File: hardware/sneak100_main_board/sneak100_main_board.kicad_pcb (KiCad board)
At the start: 2 copper layers, 50 x 72 mm, 63 parts, among them J1 Conn_02x05_Counter_Clockwise, J10 Conn_01x03, J2 Conn_01x03, J3 Conn_01x06, J4 Conn_01x06, J5 Conn_01x06, J6 Conn_01x06, J7 Conn_01x03, J8 Conn_01x03, J9 Conn_01x03, Q1 SFH-313FA, Q2 SFH-313FA, Q3 SFH-313FA, Q4 SFH-313FA, Q5 SFH-313FA, Q6 SFH-313FA, SW1 SW_Push, SW2 SW_Push, U1 DRV8835, U2 DRV8835, U3 DRV8835, U4 DRV8835, U5 CD4051B, U6 CD4051B

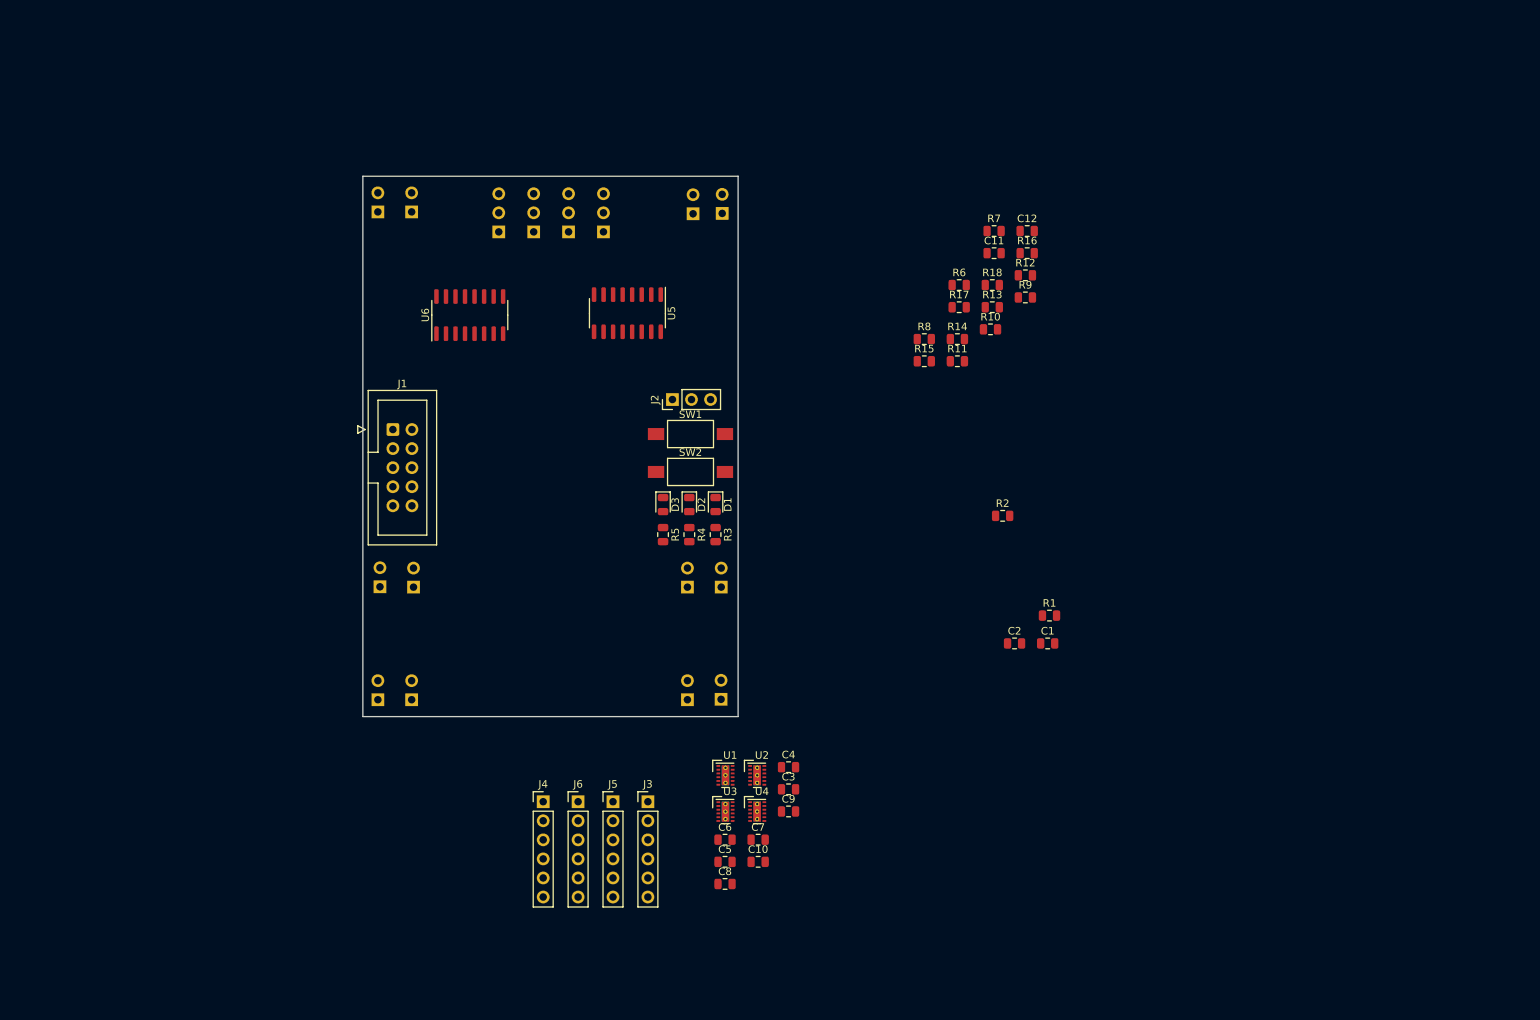
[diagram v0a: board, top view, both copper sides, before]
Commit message: Add stm32f405 uC scheme
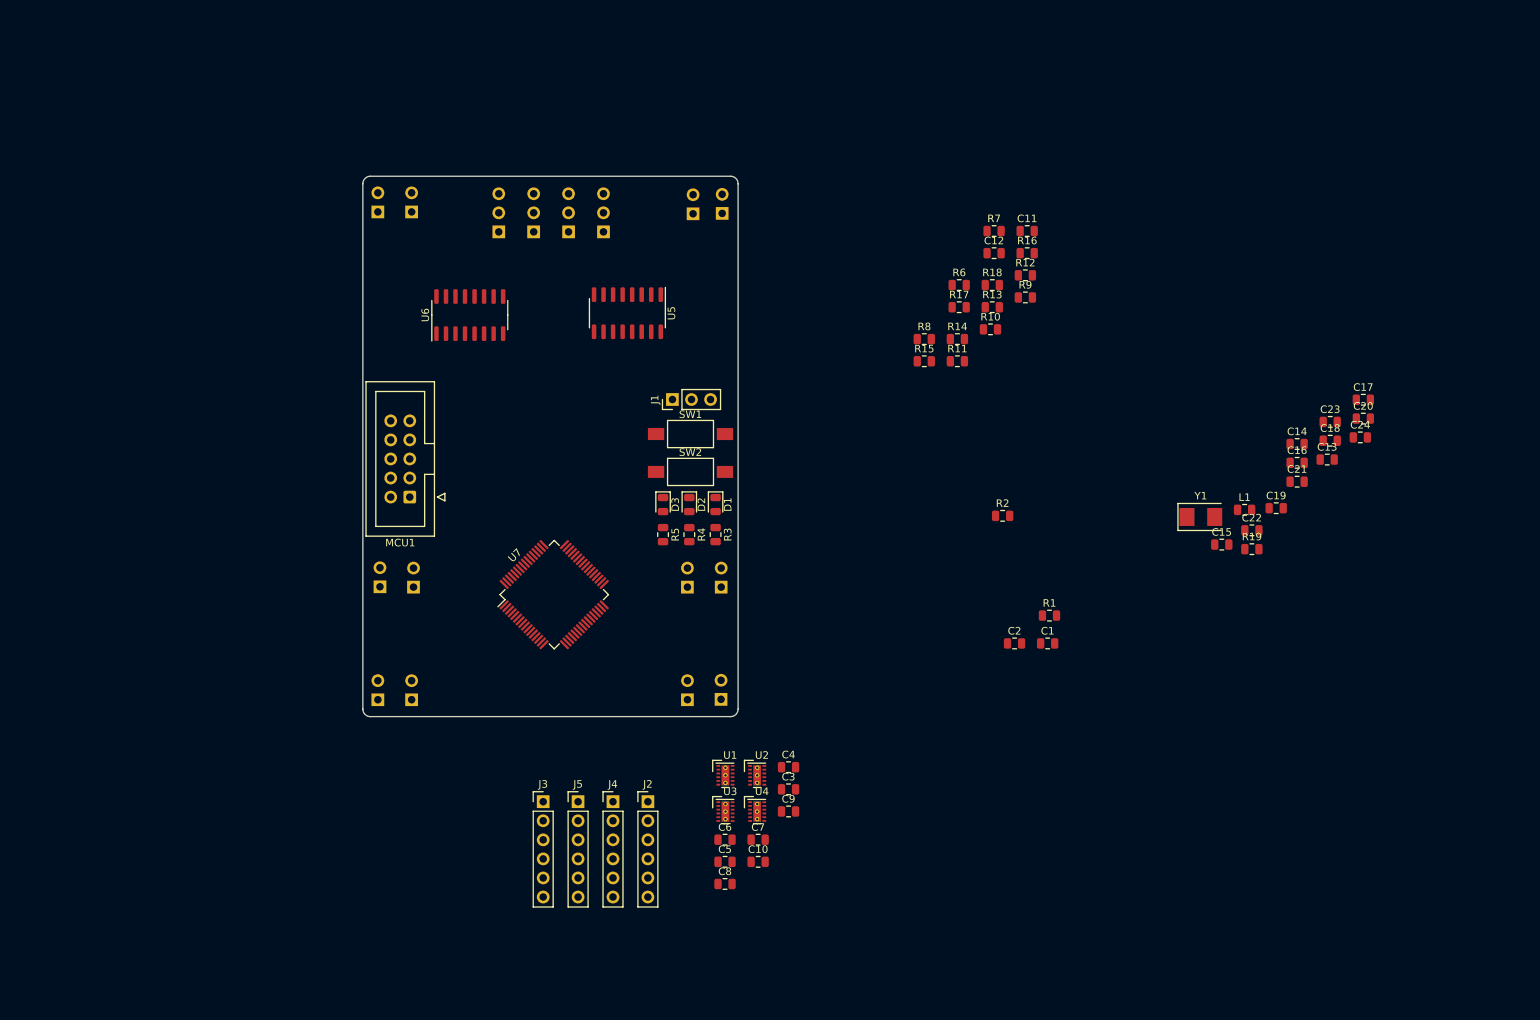
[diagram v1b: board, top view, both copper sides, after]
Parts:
- removed the J1 at (126.8, 75.2)
- added C13: 100nF, Capacitor_SMD:C_0805_2012Metric, F.Cu at (251.2, 79.2)
- added C14: 2.2uF, Capacitor_SMD:C_0805_2012Metric, F.Cu at (247.2, 77.2)
- added C15: 2.2uF, Capacitor_SMD:C_0805_2012Metric, F.Cu at (237.2, 90.6)
- added C16: 1uF, Capacitor_SMD:C_0805_2012Metric, F.Cu at (247.2, 79.7)
- added C17: 100nF, Capacitor_SMD:C_0805_2012Metric, F.Cu at (256.1, 71.3)
- added C18: 20pF, Capacitor_SMD:C_0805_2012Metric, F.Cu at (251.7, 76.7)
- added C19: 20pF, Capacitor_SMD:C_0805_2012Metric, F.Cu at (244.4, 85.7)
- added C20: 100nF, Capacitor_SMD:C_0805_2012Metric, F.Cu at (256.1, 73.8)
- added C21: 100nF, Capacitor_SMD:C_0805_2012Metric, F.Cu at (247.2, 82.2)
- added C22: 100nF, Capacitor_SMD:C_0805_2012Metric, F.Cu at (241.2, 88.7)
- added C23: 100nF, Capacitor_SMD:C_0805_2012Metric, F.Cu at (251.7, 74.2)
- added C24: 4.7uF, Capacitor_SMD:C_0805_2012Metric, F.Cu at (255.7, 76.3)
- added L1: 4.7uH, Inductor_SMD:L_0805_2012Metric, F.Cu at (240.2, 86.0)
- added MCU1: Conn_02x05_Counter_Clockwise, Connector_IDC:IDC-Header_2x05_P2.54mm_Vertical, F.Cu at (129.0, 84.2)
- added R19: 10k, Resistor_SMD:R_0805_2012Metric, F.Cu at (241.2, 91.2)
- added U7: STM32F405RGTx, Package_QFP:LQFP-64_10x10mm_P0.5mm, F.Cu at (148.2, 97.2)
- added Y1: 8MHz, Crystal:Crystal_SMD_5032-2Pin_5.0x3.2mm, F.Cu at (234.4, 86.9)
- renumbered C12 to C11, C11 to C12, J2 to J1, J3 to J2, J4 to J3, J5 to J4, J6 to J5, J7 to J6, J8 to J7, J9 to J8, J10 to J9
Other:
- outline, holes or cut-outs redrawn

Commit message: Hardware configuration schematic
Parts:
- added C3: 4.7uF, Capacitor_SMD:CP_Elec_4x3, F.Cu at (250.2, 102.2)
- added J2: Conn_01x06, Connector_PinSocket_2.54mm:PinSocket_1x06_P2.54mm_Vertical, F.Cu at (229.1, 101.7)
- added J3: Conn_01x04, Connector_PinSocket_2.54mm:PinSocket_1x04_P2.54mm_Vertical, F.Cu at (233.7, 101.7)
- added J4: Conn_01x02, Connector_PinHeader_2.54mm:PinHeader_1x02_P2.54mm_Vertical, F.Cu at (248.7, 107.5)
- added R24: 4k7, Resistor_SMD:R_0805_2012Metric, F.Cu at (234.5, 80.2)
- added R25: 4k7, Resistor_SMD:R_0805_2012Metric, F.Cu at (238.9, 80.2)
- added R6: 100, Resistor_SMD:R_0805_2012Metric, F.Cu at (233.5, 113.0)
- added R7: 10k, Resistor_SMD:R_0805_2012Metric, F.Cu at (242.8, 108.3)
- added R8: 22, Resistor_SMD:R_0805_2012Metric, F.Cu at (242.8, 111.3)
- added R9: 22, Resistor_SMD:R_0805_2012Metric, F.Cu at (256.3, 100.8)
- added U1: TSOP4838, Connector_PinHeader_2.54mm:PinHeader_1x03_P2.54mm_Vertical, F.Cu at (238.2, 109.2)
- J1: value Conn_01x03 -> USB_OTG; footprint Connector_PinHeader_2.54mm:PinHeader_1x03_P2.54mm_Vertical -> Connector_USB:USB_Micro-B_Molex_47346-0001
- moved J1 42.5 mm to (148.2, 110.8), turned to 0 degrees
- moved D9 25.6 mm to (195.0, 118.5)
- moved Q6 25.6 mm to (190.5, 118.5)
- moved D8 19.2 mm to (106.5, 117.2)
- moved Q5 19.2 mm to (111.0, 117.2)
- moved C11 16.7 mm to (160.2, 139.6)
- moved C4 16.7 mm to (164.2, 129.9)
- moved C5 16.7 mm to (164.2, 127.0)
- moved C6 16.7 mm to (155.8, 139.6)
- moved C7 16.7 mm to (155.8, 136.7)
- moved C8 16.7 mm to (160.2, 136.7)
- moved C9 16.7 mm to (155.8, 142.6)
- moved J5 16.7 mm to (145.5, 131.6)
- moved J6 16.7 mm to (131.5, 131.6)
- moved J7 16.7 mm to (140.8, 131.6)
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- renumbered C9 to C10, C10 to C11, C11 to C12, C12 to C13, C13 to C14, C14 to C15, C15 to C16, C16 to C17, C17 to C18, C18 to C19, C19 to C20, C20 to C21, C21 to C22, C22 to C23, C23 to C24, C24 to C25, C3 to C4, C4 to C5, C5 to C6, C6 to C7, C7 to C8, C8 to C9, J7 to J10, J8 to J11, J9 to J12, J2 to J5, J3 to J6, J4 to J7, J5 to J8, J6 to J9, R3 to R1, R6 to R10, R7 to R11, R8 to R12, R9 to R13, R10 to R14, R11 to R15, R12 to R16, R13 to R17, R14 to R18, R15 to R19, R1 to R2, R16 to R20, R17 to R21, R18 to R22, R19 to R23, R2 to R3, U1 to U2, U2 to U3, U3 to U4, U4 to U5, U5 to U6, U6 to U7, U7 to U8
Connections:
- C14 pad 1: /controller/RESET -> /interface/BUTTON2
- J1 pad 2: (no net) -> Net-(J1-Pad2)
- J1 pad 3: GND -> Net-(J1-Pad3)
- J10 pad 1: (no net) -> /controller/LINE_LM
- J11 pad 1: (no net) -> /controller/LINE_RM
- J12 pad 1: (no net) -> /controller/LINE_RR
- J5 pad 2: (no net) -> /controller/LF_B
- J5 pad 3: (no net) -> /controller/LF_A
- J6 pad 2: (no net) -> /controller/RF_B
- J6 pad 3: (no net) -> /controller/RF_A
- J7 pad 2: (no net) -> /controller/LB_B
- J7 pad 3: (no net) -> /controller/LB_A
- J8 pad 2: (no net) -> /controller/RB_B
- J8 pad 3: (no net) -> /controller/RB_A
- J9 pad 1: (no net) -> /controller/LINE_LL
- MCU1 pad 1: /controller/RESET -> /interface/BUTTON2
- R1 pad 2: (no net) -> /interface/LED1
- R22 pad 1: /proximitySensors/TX_ENABLE -> /controller/PROXIMITY_TX_ENABLE
- R23 pad 2: /controller/RESET -> /interface/BUTTON2
- R4 pad 2: (no net) -> /interface/LED2
- R5 pad 2: (no net) -> /interface/LED3
- U2 pad 10: /motors/LF_IN1 -> /controller/LF_IN1
- U2 pad 7: /motors/LF_IN2 -> /controller/LF_IN2
- U2 pad 8: /motors/LF_IN1 -> /controller/LF_IN1
- U2 pad 9: /motors/LF_IN2 -> /controller/LF_IN2
- U3 pad 10: /motors/RF_IN1 -> /controller/RF_IN1
- U3 pad 7: /motors/RF_IN2 -> /controller/RF_IN2
- U3 pad 8: /motors/RF_IN1 -> /controller/RF_IN1
- U3 pad 9: /motors/RF_IN2 -> /controller/RF_IN2
- U4 pad 10: /motors/LB_IN1 -> /controller/LB_IN1
- U4 pad 7: /motors/LB_IN2 -> /controller/LB_IN2
- U4 pad 8: /motors/LB_IN1 -> /controller/LB_IN1
- U4 pad 9: /motors/LB_IN2 -> /controller/LB_IN2
- U5 pad 10: /motors/RB_IN1 -> /controller/RB_IN1
- U5 pad 7: /motors/RB_IN2 -> /controller/RB_IN2
- U5 pad 8: /motors/RB_IN1 -> /controller/RB_IN1
- U5 pad 9: /motors/RB_IN2 -> /controller/RB_IN2
- U6 pad 6: /proximitySensors/TX_ENABLE -> /controller/PROXIMITY_TX_ENABLE
- U7 pad 3: (no net) -> /controller/PROXIMITY_RX_READ
- U8 pad 10: (no net) -> /controller/LINE_RM
- U8 pad 11: (no net) -> /controller/LINE_RR
- U8 pad 14: (no net) -> /controller/RF_A
- U8 pad 15: (no net) -> /controller/RF_B
- U8 pad 16: (no net) -> /interface/BLUETOOTH_RX
- U8 pad 17: (no net) -> /interface/BLUETOOTH_TX
- U8 pad 2: (no net) -> /controller/MODULE_START
- U8 pad 22: (no net) -> /controller/LB_A
- U8 pad 23: (no net) -> /controller/LB_B
- U8 pad 25: (no net) -> /controller/PROXIMITY_RX_READ
- U8 pad 26: (no net) -> /controller/LB_IN1
- U8 pad 27: (no net) -> /controller/LB_IN2
- U8 pad 29: (no net) -> /controller/RF_IN1
- U8 pad 3: (no net) -> /controller/MODULE_KILL
- U8 pad 30: (no net) -> /controller/RF_IN2
- U8 pad 35: (no net) -> /controller/LF_IN1
- U8 pad 36: (no net) -> /controller/LF_IN2
- U8 pad 37: (no net) -> /controller/LF_A
- U8 pad 38: (no net) -> /controller/LF_B
- U8 pad 39: (no net) -> /controller/PROXIMITY_TX_ENABLE
- U8 pad 40: (no net) -> /controller/I2C3_SDA
- U8 pad 41: (no net) -> /controller/I2C3_SCL
- U8 pad 44: (no net) -> /controller/USB_DM
- U8 pad 45: (no net) -> /controller/USB_DP
- U8 pad 50: (no net) -> /interface/LED1
- U8 pad 51: (no net) -> /interface/LED2
- U8 pad 52: (no net) -> /interface/LED3
- U8 pad 53: (no net) -> /interface/BUTTON1
- U8 pad 54: (no net) -> /controller/RECEIVER_OUT
- U8 pad 55: (no net) -> /proximitySensors/ADD0
- U8 pad 56: (no net) -> /proximitySensors/ADD1
- U8 pad 57: (no net) -> /proximitySensors/ADD2
- U8 pad 58: (no net) -> /controller/RB_A
- U8 pad 59: (no net) -> /controller/RB_B
- U8 pad 61: (no net) -> /controller/RB_IN1
- U8 pad 62: (no net) -> /controller/RB_IN2
- U8 pad 7: /controller/RESET -> /interface/BUTTON2
- U8 pad 8: (no net) -> /controller/LINE_LL
- U8 pad 9: (no net) -> /controller/LINE_LM

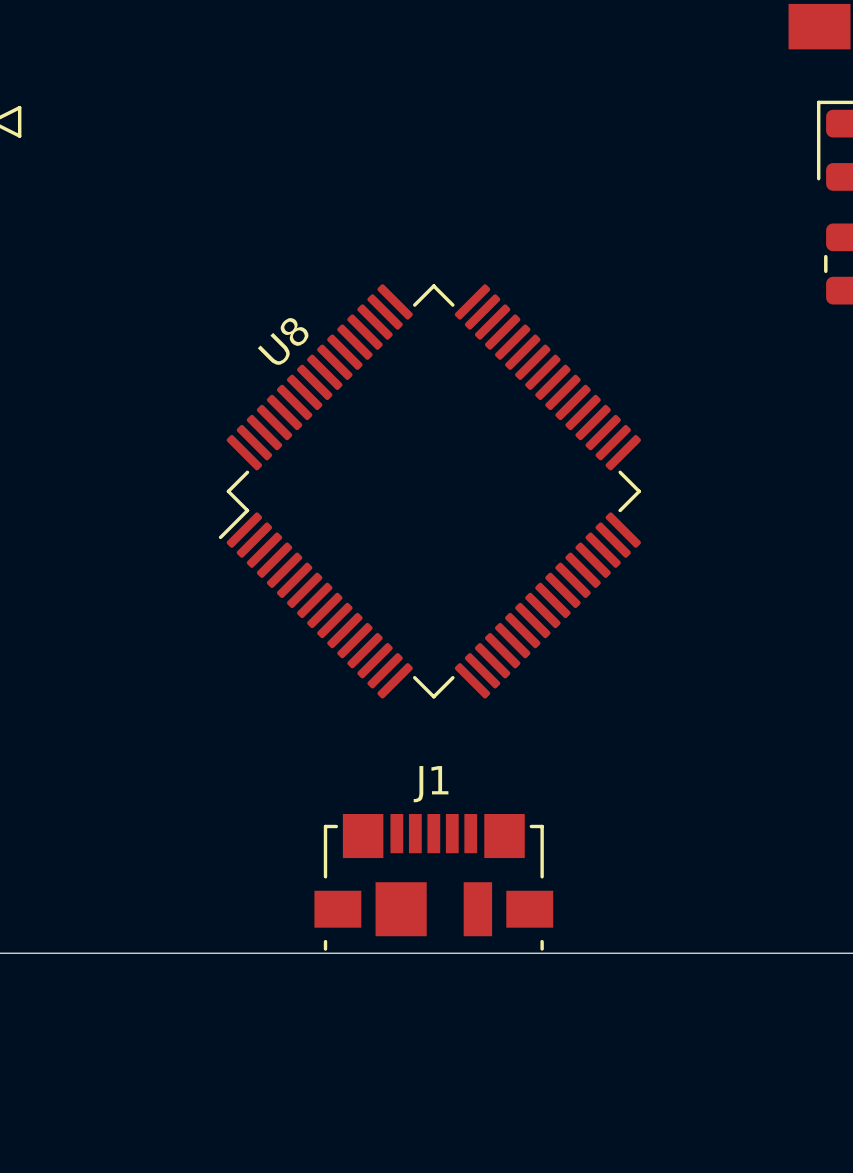
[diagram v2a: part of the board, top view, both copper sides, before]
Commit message: Change usb connector footprint
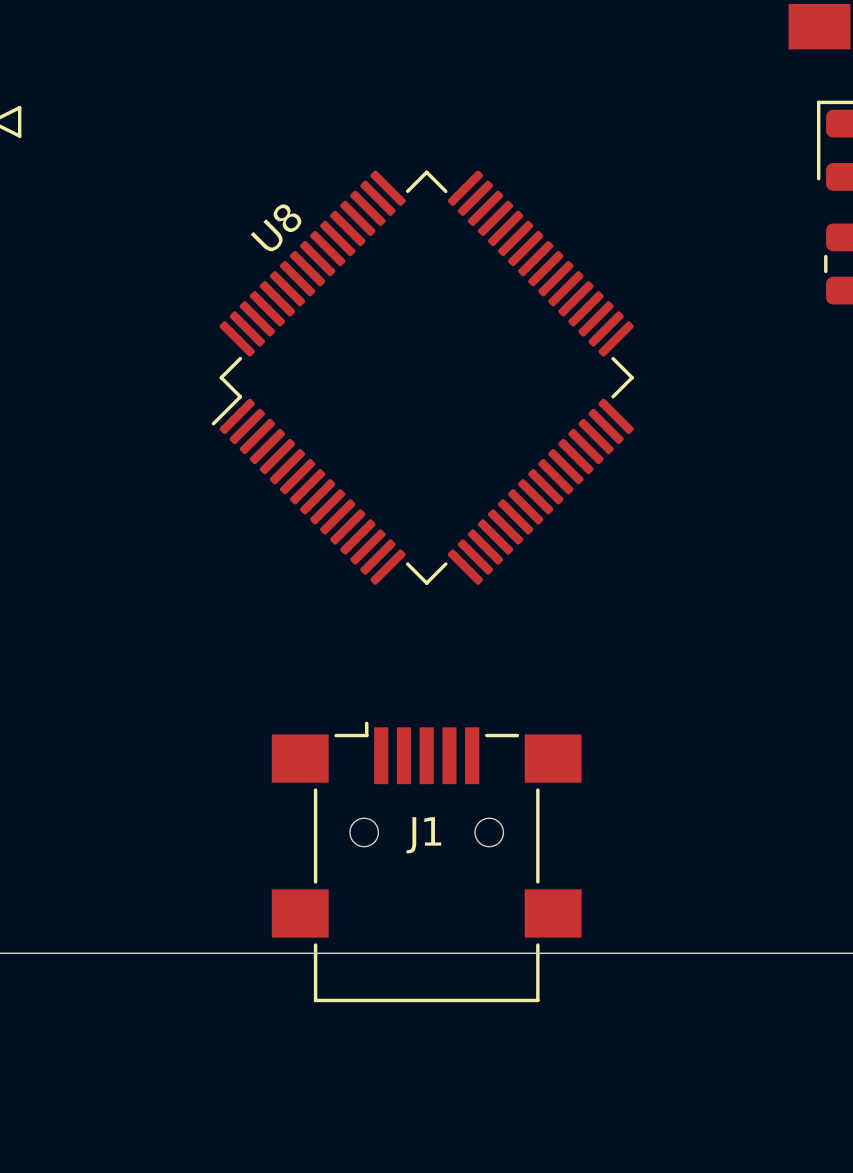
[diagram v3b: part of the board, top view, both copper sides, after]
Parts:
- J1: footprint Connector_USB:USB_Micro-B_Molex_47346-0001 -> Connector_USB:USB_Mini-B_Lumberg_2486_01_Horizontal
- moved U8 4.01 mm to (148.0, 93.2)
- moved J1 1.52 mm to (148.0, 109.2)

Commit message: Power section scheme
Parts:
- added C12: 100nF, Capacitor_SMD:C_0603_1608Metric, F.Cu at (251.8, 59.2)
- added C13: 4.7uF, Capacitor_SMD:CP_Elec_4x3, F.Cu at (243.7, 49.2)
- added C14: 4.7uF, Capacitor_SMD:CP_Elec_4x3, F.Cu at (237.8, 59.0)
- added C15: 100nF, Capacitor_SMD:C_0603_1608Metric, F.Cu at (255.8, 57.2)
- added D4: LED, LED_SMD:LED_0603_1608Metric, F.Cu at (254.2, 47.5)
- added D5: LED, LED_SMD:LED_0603_1608Metric, F.Cu at (243.7, 57.9)
- added D6: LED, LED_SMD:LED_0603_1608Metric, F.Cu at (236.0, 63.2)
- added J10: Conn_01x02, Connector_PinHeader_2.54mm:PinHeader_1x02_P2.54mm_Vertical, F.Cu at (249.9, 48.6)
- added J9: Conn_01x03, Connector_PinHeader_2.54mm:PinHeader_1x03_P2.54mm_Vertical, F.Cu at (237.5, 48.6)
- added Q1: Q_PMOS_DGS, Package_TO_SOT_SMD:SOT-23, F.Cu at (243.9, 54.4)
- added Q2: Q_PMOS_DGS, Package_TO_SOT_SMD:SOT-23, F.Cu at (248.4, 55.7)
- added R10: 4k7, Resistor_SMD:R_0603_1608Metric, F.Cu at (244.0, 63.0)
- added R11: 1k, Resistor_SMD:R_0603_1608Metric, F.Cu at (252.6, 54.7)
- added R12: 1k, Resistor_SMD:R_0603_1608Metric, F.Cu at (240.0, 63.1)
- added R13: R, Resistor_SMD:R_0603_1608Metric, F.Cu at (243.7, 60.5)
- added R14: 1.5k, Resistor_SMD:R_0603_1608Metric, F.Cu at (254.2, 50.1)
- added R15: 680, Resistor_SMD:R_0603_1608Metric, F.Cu at (247.7, 59.2)
- added R16: 340, Resistor_SMD:R_0603_1608Metric, F.Cu at (248.0, 61.8)
- added R17: R, Resistor_SMD:R_0603_1608Metric, F.Cu at (252.0, 61.8)
- added SW3: SW_Push_SPDT, Button_Switch_SMD:SW_SPDT_CK-JS102011SAQN, F.Cu at (229.6, 51.3)
- added U6: LM1117-3.3, Package_TO_SOT_SMD:SOT-223-3_TabPin2, F.Cu at (229.0, 60.2)
- C1, C10, C11, C2, C4, C5, C6, C7, C8, C9: footprint Capacitor_SMD:C_0805_2012Metric -> Capacitor_SMD:C_0603_1608Metric
- C16: renamed from C12; footprint Capacitor_SMD:C_0805_2012Metric -> Capacitor_SMD:C_0603_1608Metric
- C17: renamed from C13; footprint Capacitor_SMD:C_0805_2012Metric -> Capacitor_SMD:C_0603_1608Metric
- C18: renamed from C14; footprint Capacitor_SMD:C_0805_2012Metric -> Capacitor_SMD:C_0603_1608Metric
- C19: renamed from C15; footprint Capacitor_SMD:C_0805_2012Metric -> Capacitor_SMD:C_0603_1608Metric
- C20: renamed from C16; footprint Capacitor_SMD:C_0805_2012Metric -> Capacitor_SMD:C_0603_1608Metric
- C21: renamed from C17; footprint Capacitor_SMD:C_0805_2012Metric -> Capacitor_SMD:C_0603_1608Metric
- C22: renamed from C18; footprint Capacitor_SMD:C_0805_2012Metric -> Capacitor_SMD:C_0603_1608Metric
- C23: renamed from C19; footprint Capacitor_SMD:C_0805_2012Metric -> Capacitor_SMD:C_0603_1608Metric
- C24: renamed from C20; footprint Capacitor_SMD:C_0805_2012Metric -> Capacitor_SMD:C_0603_1608Metric
- C25: renamed from C21; footprint Capacitor_SMD:C_0805_2012Metric -> Capacitor_SMD:C_0603_1608Metric
- C26: renamed from C22; footprint Capacitor_SMD:C_0805_2012Metric -> Capacitor_SMD:C_0603_1608Metric
- C27: renamed from C23; footprint Capacitor_SMD:C_0805_2012Metric -> Capacitor_SMD:C_0603_1608Metric
- C28: renamed from C24; footprint Capacitor_SMD:C_0805_2012Metric -> Capacitor_SMD:C_0603_1608Metric
- D1, D2, D3: footprint LED_SMD:LED_0805_2012Metric -> LED_SMD:LED_0603_1608Metric
- renumbered C25 to C29, D7 to D10, D8 to D11, D9 to D12, D4 to D7, D5 to D8, D6 to D9, J9 to J11, J10 to J12, J11 to J13, J12 to J14, Q1 to Q3, Q2 to Q4, Q3 to Q5, Q4 to Q6, Q5 to Q7, Q6 to Q8, R10 to R18, R11 to R19, R12 to R20, R13 to R21, R14 to R22, R15 to R23, R16 to R24, R17 to R25, R18 to R26, R19 to R27, R20 to R28, R21 to R29, R22 to R31, R23 to R32, R24 to R33, R25 to R34, U6 to U7, U7 to U8, U8 to U9
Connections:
- net VIN renamed SUPPLY
- J2 pad 2: (no net) -> +5V
- U9 pad 24: (no net) -> /controller/BATTERY_SENSE
